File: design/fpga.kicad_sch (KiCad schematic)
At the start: 83 parts, among them J7 DEBUG_FPGA_GPIO, J8 DIGILENT_JTAG_HS2_01X06, SW1 RST, SW2 PROG, U13 XC7S15-FTGB196, U14 IS25LP064A-JKx

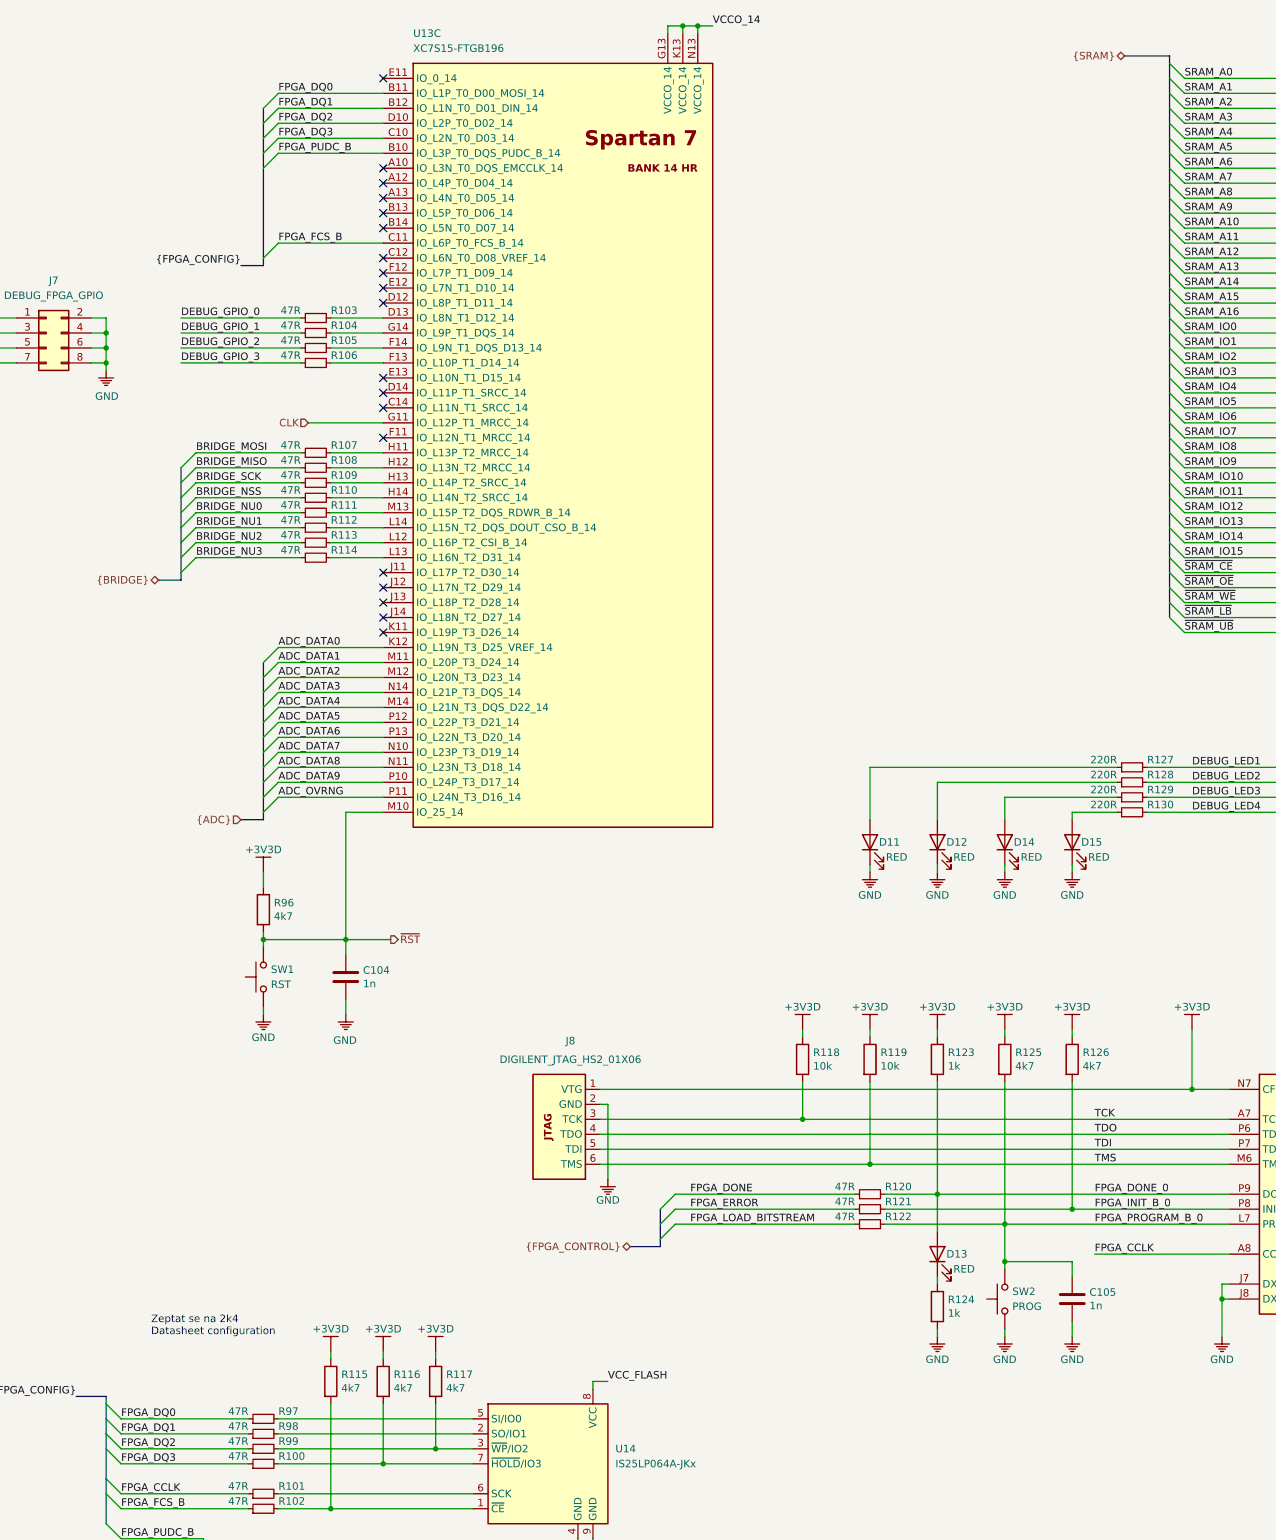
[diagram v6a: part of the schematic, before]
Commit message: Moved FPGA capacitors
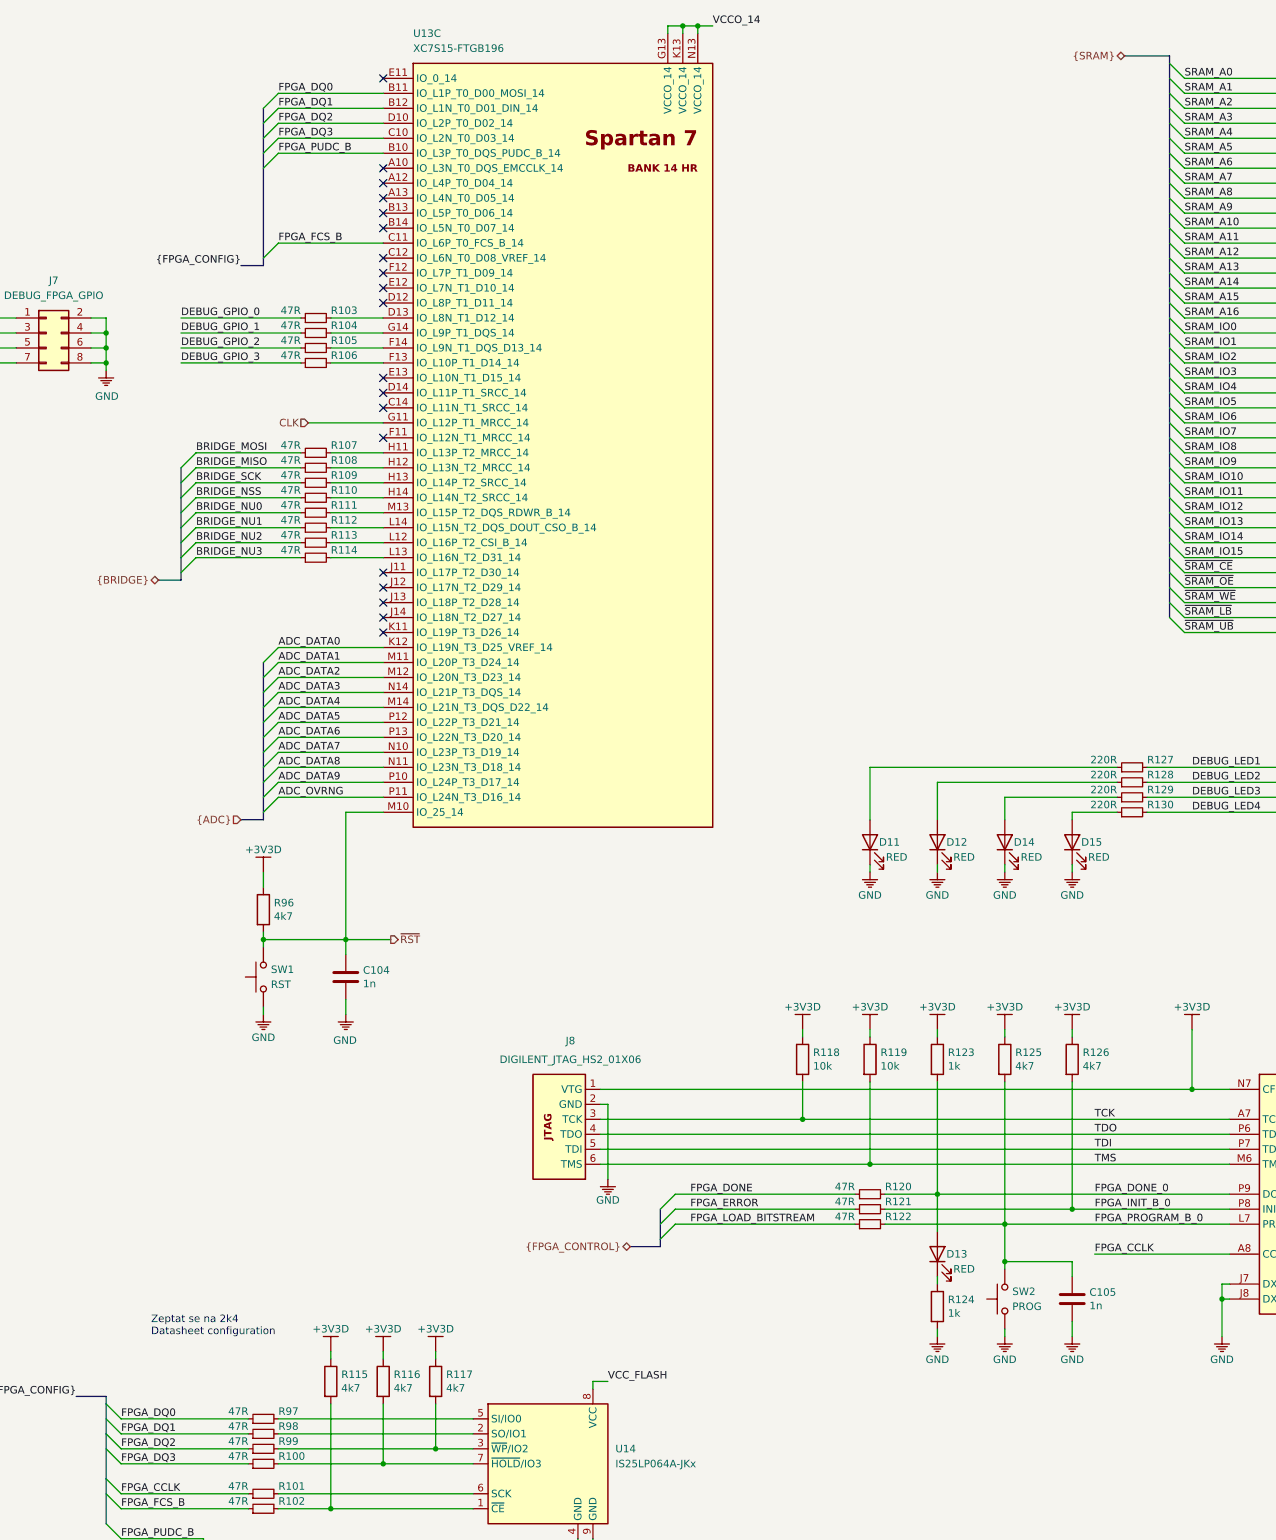
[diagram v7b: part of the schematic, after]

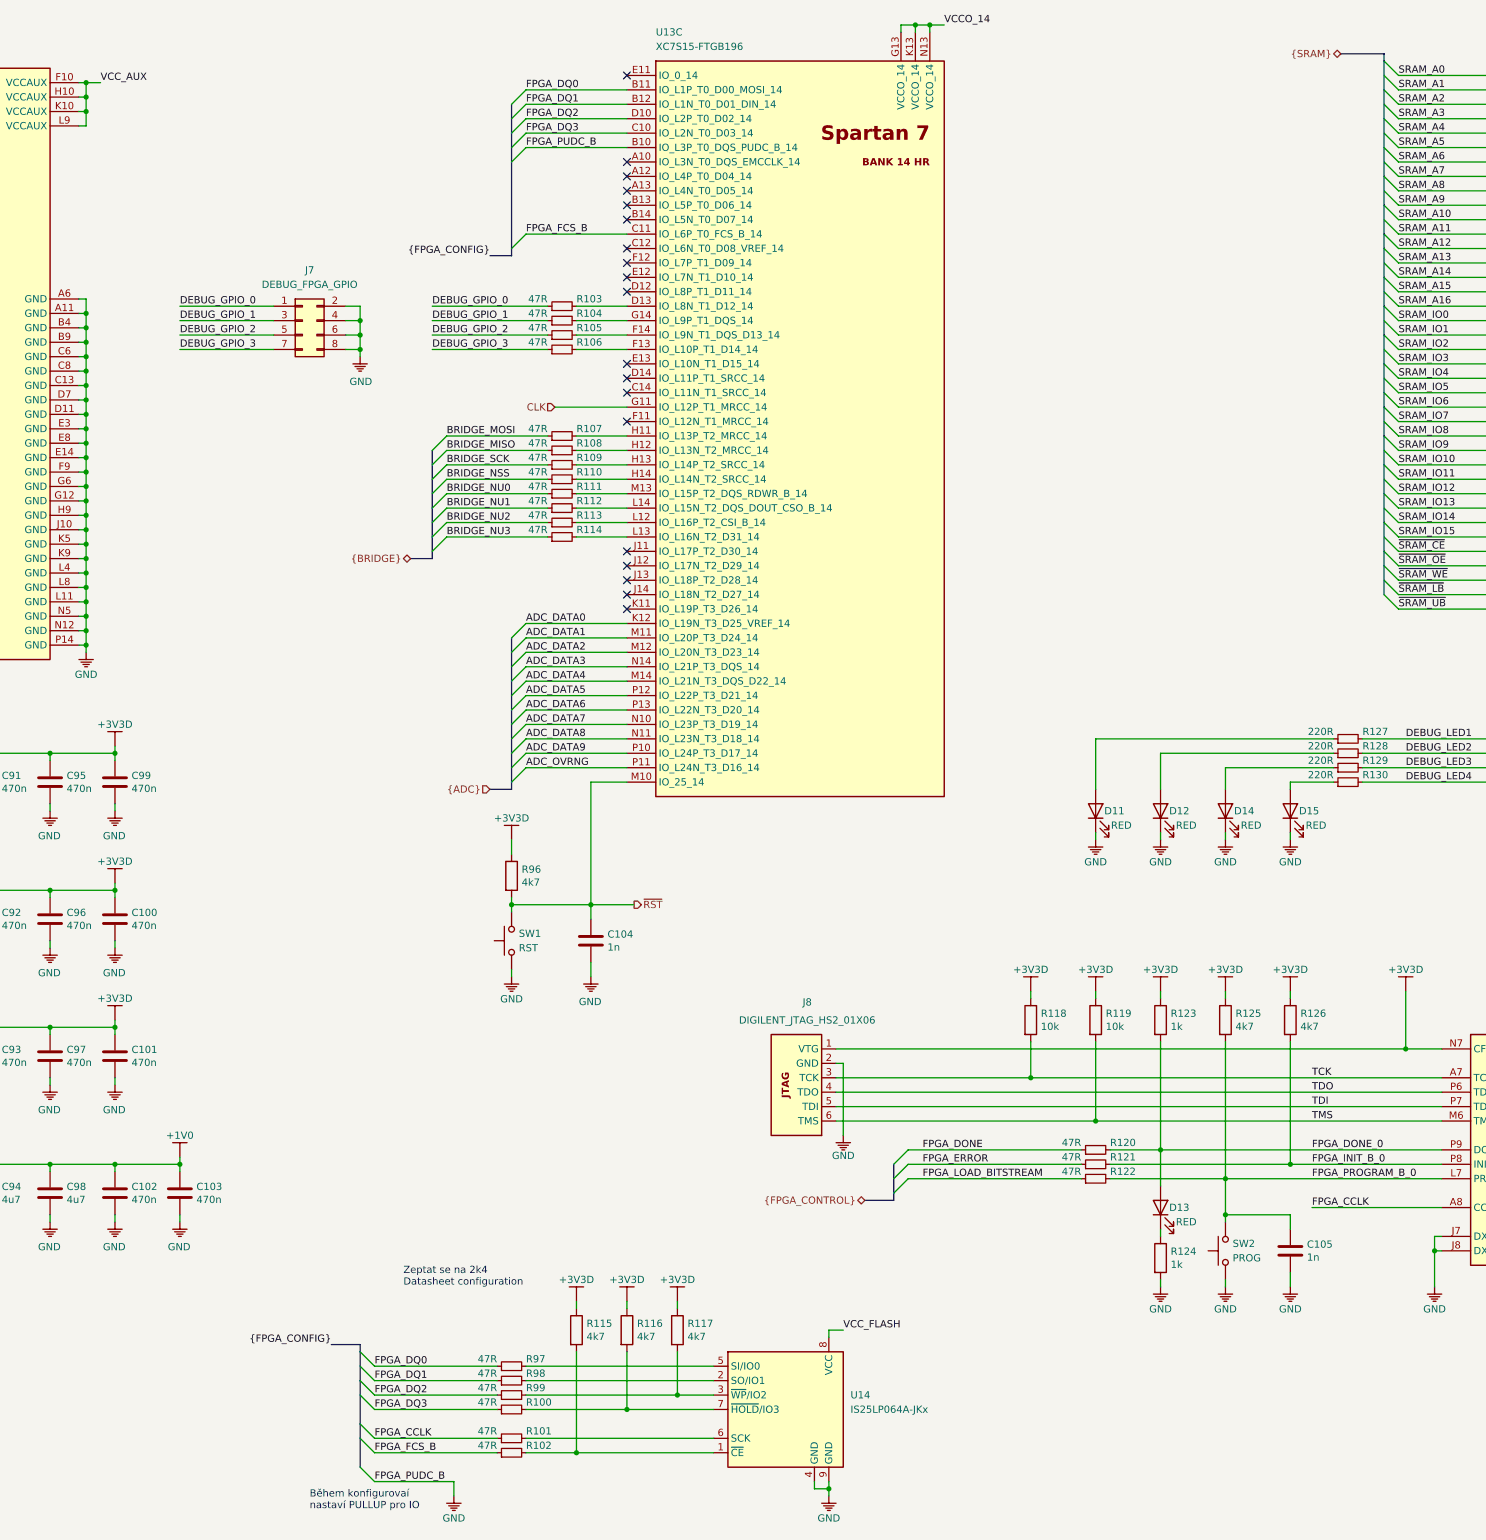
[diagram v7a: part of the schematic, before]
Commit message: Added some polygons and connected ADC
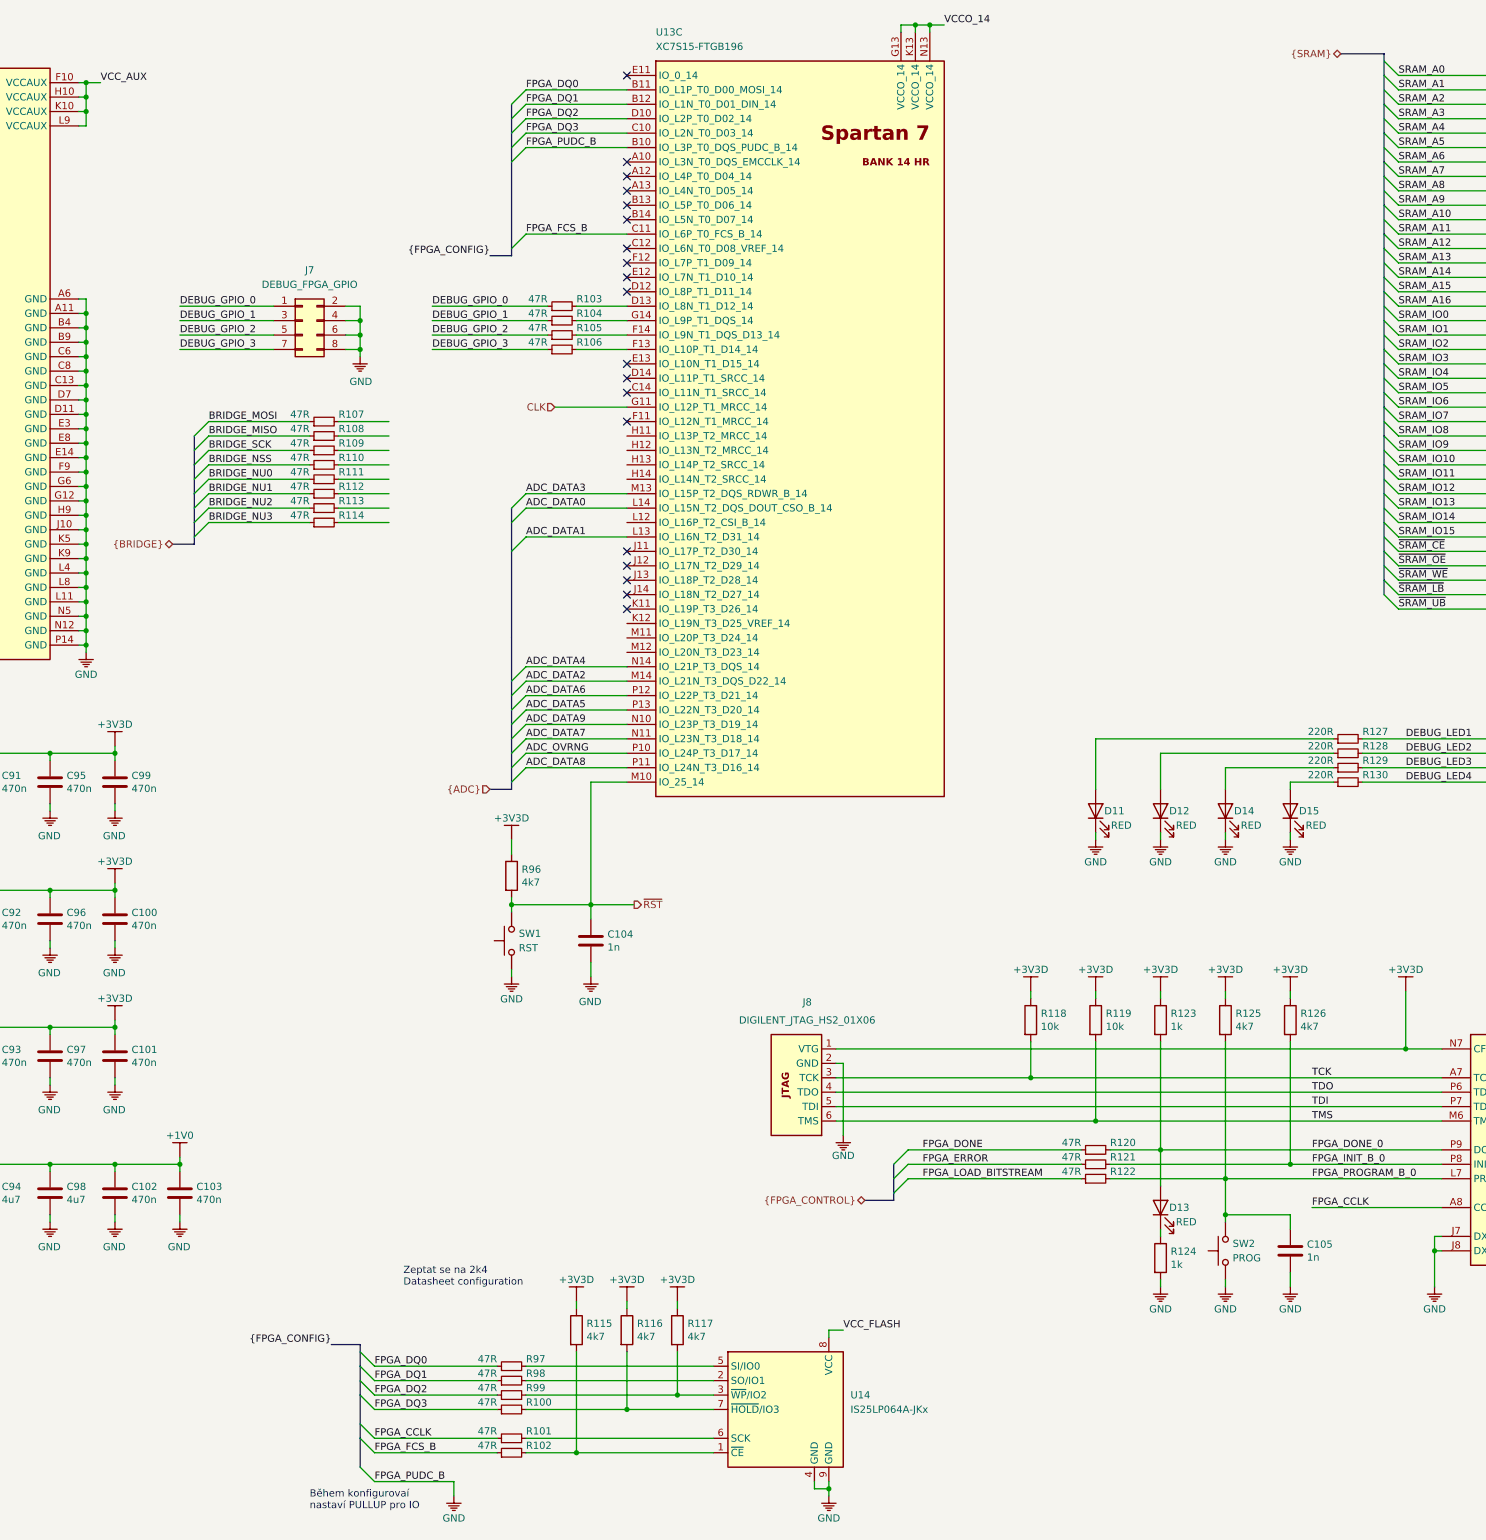
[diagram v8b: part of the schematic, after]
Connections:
- net ADC_DATA0: now also U13.L14 (IO_L15N_T2_DQS_DOUT_CSO_B_14); no longer U13.K12 (IO_L19N_T3_D25_VREF_14)
- net ADC_DATA1: now also U13.L13 (IO_L16N_T2_D31_14); no longer U13.M11 (IO_L20P_T3_D24_14)
- net ADC_DATA2: now also U13.M14 (IO_L21N_T3_DQS_D22_14); no longer U13.M12 (IO_L20N_T3_D23_14)
- net ADC_DATA3: now also U13.M13 (IO_L15P_T2_DQS_RDWR_B_14); no longer U13.N14 (IO_L21P_T3_DQS_14)
- net ADC_DATA4: now also U13.N14 (IO_L21P_T3_DQS_14); no longer U13.M14 (IO_L21N_T3_DQS_D22_14)
- net ADC_DATA5: now also U13.P13 (IO_L22N_T3_D20_14); no longer U13.P12 (IO_L22P_T3_D21_14)
- net ADC_DATA6: now also U13.P12 (IO_L22P_T3_D21_14); no longer U13.P13 (IO_L22N_T3_D20_14)
- net ADC_DATA7: now also U13.N11 (IO_L23N_T3_D18_14); no longer U13.N10 (IO_L23P_T3_D19_14)
- net ADC_DATA8: now also U13.P11 (IO_L24N_T3_D16_14); no longer U13.N11 (IO_L23N_T3_D18_14)
- net ADC_DATA9: now also U13.N10 (IO_L23P_T3_D19_14); no longer U13.P10 (IO_L24P_T3_D17_14)
- net ADC_OVRNG: now also U13.P10 (IO_L24P_T3_D17_14); no longer U13.P11 (IO_L24N_T3_D16_14)
- net at R107.2: no longer U13.H11 (IO_L13P_T2_MRCC_14)
- net at R111.2: no longer U13.M13 (IO_L15P_T2_DQS_RDWR_B_14)
- net at U13.H12 (IO_L13N_T2_MRCC_14): no longer R108.2
- net at U13.H13 (IO_L14P_T2_SRCC_14): no longer R109.2
- net at U13.H14 (IO_L14N_T2_SRCC_14): no longer R110.2
- net at U13.L12 (IO_L16P_T2_CSI_B_14): no longer R113.2
- net at R114.2: no longer U13.L13 (IO_L16N_T2_D31_14)
- net at R112.2: no longer U13.L14 (IO_L15N_T2_DQS_DOUT_CSO_B_14)
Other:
- moved on the sheet: R107, R108, R109, R110, R111, R112, R113, R114
